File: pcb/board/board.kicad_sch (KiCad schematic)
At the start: 6 parts, among them J1 Screw_Terminal_01x03, J2 Screw_Terminal_01x03, J3 Screw_Terminal_01x03, J5 Screw_Terminal_01x03

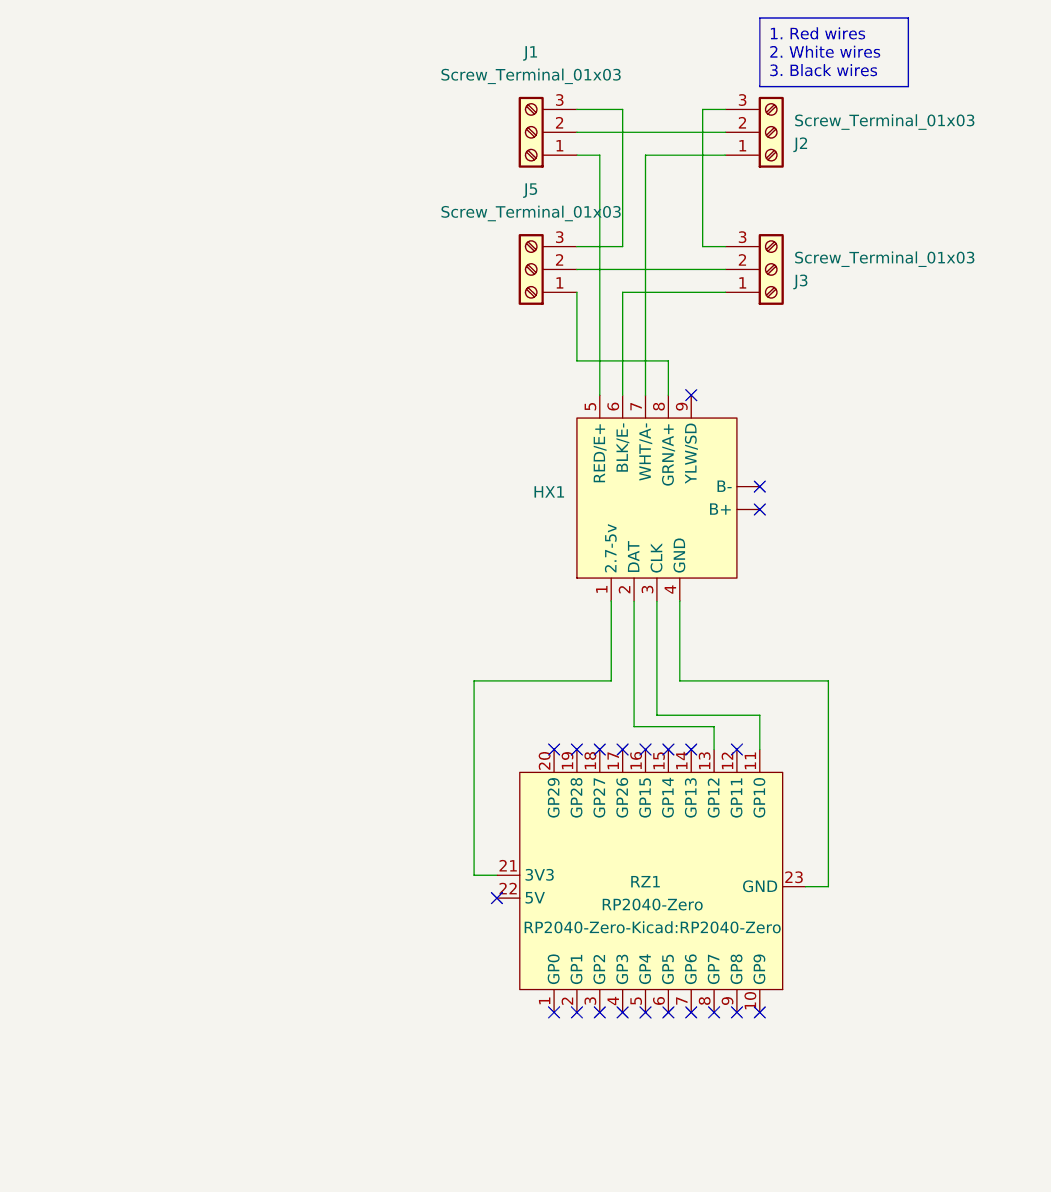
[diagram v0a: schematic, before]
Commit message: wip work on the load cell part
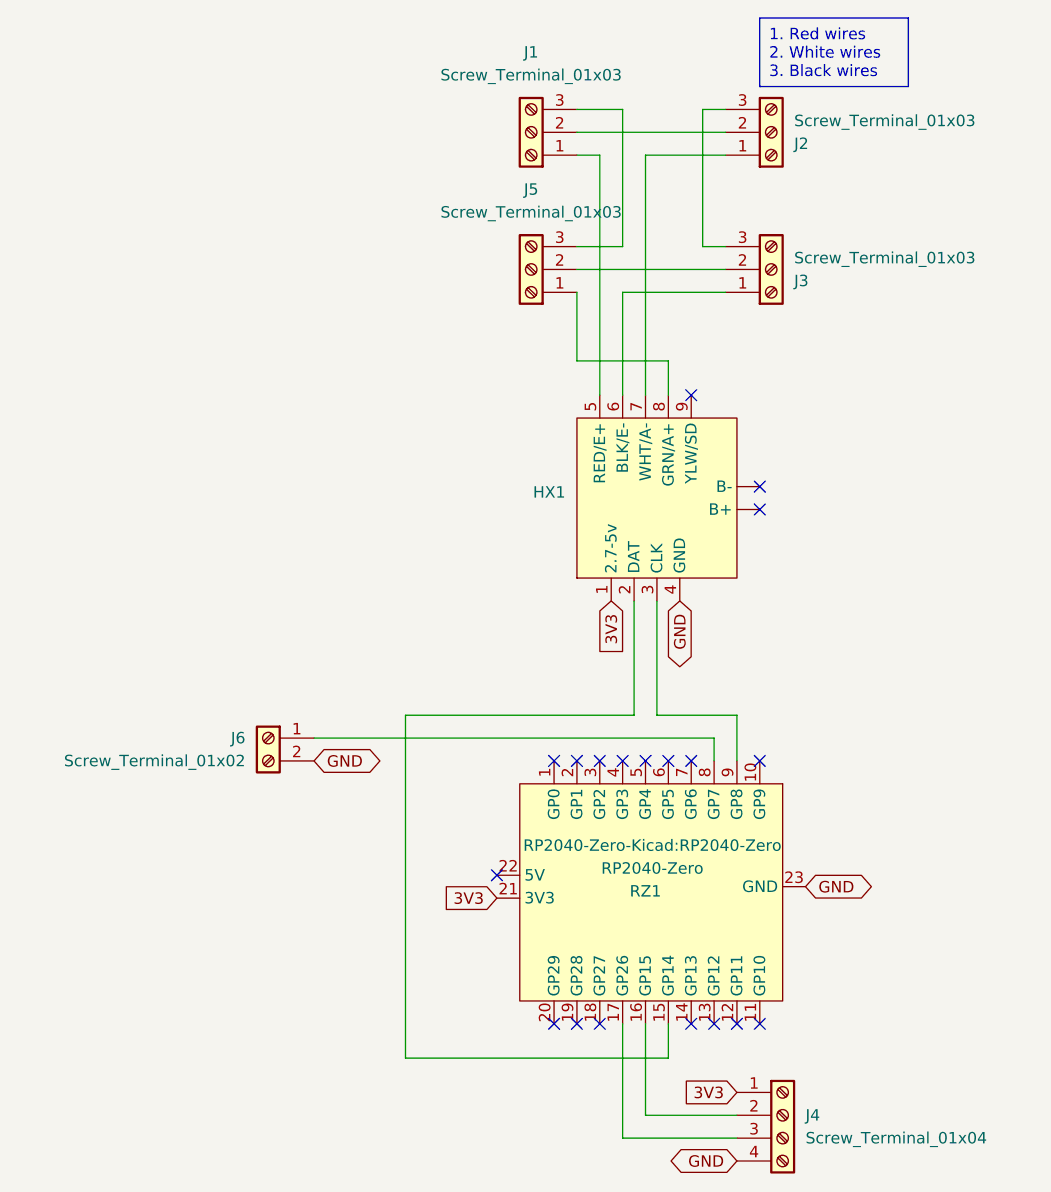
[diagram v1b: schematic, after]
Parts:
- added J4: Screw_Terminal_01x04, Connector_JST:JST_XH_B4B-XH-A_1x04_P2.50mm_Vertical, symbol Connector:Screw_Terminal_01x04
- added J6: Screw_Terminal_01x02, Connector_JST:JST_XH_B2B-XH-A_1x02_P2.50mm_Vertical, symbol Connector:Screw_Terminal_01x02
- J1, J2, J3, J5: footprint TerminalBlock_MetzConnect:TerminalBlock_MetzConnect_Type011_RT05503HBWC_1x03_P5.00mm_Horizontal -> Connector_JST:JST_XH_B3B-XH-A_1x03_P2.50mm_Vertical
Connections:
- net at RZ1.11 (GP10): no longer HX1.3 (CLK)
- net at RZ1.13 (GP12): no longer HX1.2 (DAT)
- net at RZ1.15 (GP14): now also HX1.2 (DAT)
- net at RZ1.16 (GP15): now also J4.2 (Pin_2)
- net at RZ1.17 (GP26): now also J4.3 (Pin_3)
- net 3V3: now reaches HX1.1 (2.7-5v), RZ1.21 (3V3)
- net 3V3: now also J4.1 (Pin_1)
- net GND: now reaches HX1.4 (GND), RZ1.23 (GND)
- net GND: now also J4.4 (Pin_4), J6.2 (Pin_2)
- net at RZ1.8 (GP7): now also J6.1 (Pin_1)
- net at RZ1.9 (GP8): now also HX1.3 (CLK)
- no-connect marks 22 -> 19
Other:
- moved on the sheet: RZ1
